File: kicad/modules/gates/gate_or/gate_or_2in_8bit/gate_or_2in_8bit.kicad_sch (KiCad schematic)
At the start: 0 parts

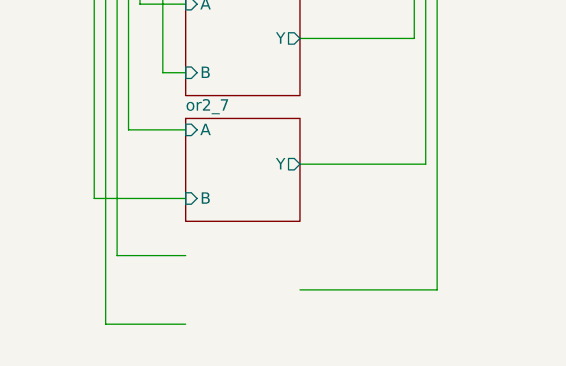
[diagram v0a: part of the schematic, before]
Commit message: Fix KiCad file paths and complete core circuit design
- Fixed file path errors across all KiCad schematics and projects
- Completed core circuit designs:
  * Adder and subtractor modules (adder2, adder8)
  * LED panels (led_panel_1) with display circuits
  * Flag LED circuits for status indicators
  * All dependent logic gate modules (AND, OR, NOT, NAND, NOR, XOR)
  * All multiplexer modules (2:1, 4:1, 8:1, 8-bit)
  * Main control board schematics
  * Flags board schematics
- Updated .gitignore to exclude KiCad backups, cache files, and lock files
- Ready for pin placement and routing of control buses, power rails, and inter-board signals
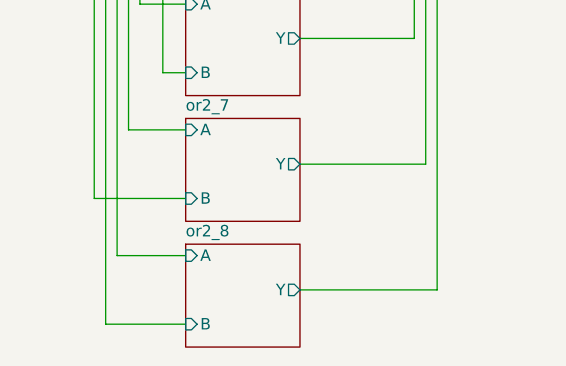
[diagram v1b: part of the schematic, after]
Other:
- added sheet or2_8 (../gate_or_2in/gate_or_2in.kicad_sch)
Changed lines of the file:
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@@
+	)
+	(sheet
+		(at 59.69 120.65)
+		(size 12.7 11.43)
+		(exclude_from_sim no)
+		(in_bom yes)
+		(on_board yes)
+		(dnp no)
+		(fields_autoplaced yes)
+		(stroke
+			(width 0.1524)
+			(type solid)
+		)
+		(fill
+			(color 0 0 0 0.0000)
+		)
+		(property "Sheetname" "or2_8"
+			(at 59.69 119.9384 0)
+			(effects
+				(font
+					(size 1.27 1.27)
+				)
+				(justify left bottom)
+			)
+		)
+		(property "Sheetfile" "../gate_or_2in/gate_or_2in.kicad_sch"
+			(at 59.69 132.6646 0)
+			(effects
+				(font
+					(size 1.27 1.27)
+				)
+				(justify left top)
+				(hide yes)
+			)
+		)
+		(pin "Y" output
+			(at 72.39 125.73 0)
+			(effects
+				(font
+					(size 1.27 1.27)
+				)
+				(justify right)
+			)
+		)
+		(pin "A" input
+			(at 59.69 121.92 180)
+			(effects
+				(font
+					(size 1.27 1.27)
+				)
+				(justify left)
+			)
+		)
+		(pin "B" input
+			(at 59.69 129.54 180)
+			(effects
+				(font
+					(size 1.27 1.27)
+				)
+				(justify left)
+			)
+		)
+		(instances
+			(project "gate_or_2in_8bit"
+				(path "/d541a682-fa01-47a3-834a-d48fe819bd53"
+					(page "9")
+				)
+			)
+		)
 	)
 	(sheet
